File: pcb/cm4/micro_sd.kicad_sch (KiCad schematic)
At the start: 5 parts, among them J501 Micro_SD_Card, U501 RT9742GGJ5

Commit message: update pcb
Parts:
- C401: renamed from C501; footprint (none) -> Capacitor_SMD:C_0805_2012Metric
- C402: renamed from C502; footprint (none) -> Capacitor_SMD:C_0805_2012Metric
- J401: renamed from J501; footprint (none) -> Connector_Card:microSD_HC_Wuerth_693072010801
- R401: renamed from R501; footprint (none) -> Resistor_SMD:R_0805_2012Metric
- renumbered U501 to U401
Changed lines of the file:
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@@
 		(dnp no)
 		(fields_autoplaced yes)
-		(property "Reference" "#PWR0501"
+		(property "Reference" "#PWR0403"
 			(at 165.1 101.6 0)
 			(effects
@@
 			(project "cm4"
 				(path "/5d20b266-567e-45c6-9e3e-145c2aea1daa/8c670a00-fcb0-468c-ba79-62d0190039f0"
-					(reference "#PWR0501")
+					(reference "#PWR0403")
 					(unit 1)
 				)
@@
 		(dnp no)
 		(fields_autoplaced yes)
-		(property "Reference" "#PWR0505"
+		(property "Reference" "#PWR0406"
 			(at 213.36 102.87 0)
 			(effects
@@
 			(project "cm4"
 				(path "/5d20b266-567e-45c6-9e3e-145c2aea1daa/8c670a00-fcb0-468c-ba79-62d0190039f0"
-					(reference "#PWR0505")
+					(reference "#PWR0406")
 					(unit 1)
 				)
@@
 		(dnp no)
 		(fields_autoplaced yes)
-		(property "Reference" "J501"
+		(property "Reference" "J401"
 			(at 123.825 71.12 0)
 			(effects
@@
 			)
 		)
-		(property "Footprint" ""
+		(property "Footprint" "Connector_Card:microSD_HC_Wuerth_693072010801"
 			(at 152.4 82.55 0)
 			(effects
@@
 			)
 		)
+		(property "LCSC" ""
+			(at 123.19 90.17 0)
+			(effects
+				(font
+					(size 1.27 1.27)
+				)
+				(hide yes)
+			)
+		)
 		(pin "3"
 		)
@@
 			(project "cm4"
 				(path "/5d20b266-567e-45c6-9e3e-145c2aea1daa/8c670a00-fcb0-468c-ba79-62d0190039f0"
-					(reference "J501")
+					(reference "J401")
 					(unit 1)
 				)
@@
 		(dnp no)
 		(fields_autoplaced yes)
-		(property "Reference" "R501"
+		(property "Reference" "R401"
 			(at 177.8 87.6299 0)
 			(effects
@@
 			)
 		)
-		(property "Footprint" ""
+		(property "Footprint" "Resistor_SMD:R_0805_2012Metric"
 			(at 173.482 88.9 90)
 			(effects
@@
 			)
 		)
+		(property "LCSC" ""
+			(at 175.26 88.9 0)
+			(effects
+				(font
+					(size 1.27 1.27)
+				)
+				(hide yes)
+			)
+		)
 		(pin "2"
 		)
@@
 			(project "cm4"
 				(path "/5d20b266-567e-45c6-9e3e-145c2aea1daa/8c670a00-fcb0-468c-ba79-62d0190039f0"
-					(reference "R501")
+					(reference "R401")
 					(unit 1)
 				)
@@
 		(dnp no)
 		(fields_autoplaced yes)
-		(property "Reference" "C502"
+		(property "Reference" "C402"
 			(at 217.17 88.8999 0)
 			(effects
@@
 			)
 		)
-		(property "Footprint" ""
+		(property "Footprint" "Capacitor_SMD:C_0805_2012Metric"
 			(at 214.3252 93.98 0)
 			(effects
@@
 			)
 		)
+		(property "LCSC" ""
+			(at 213.36 90.17 0)
+			(effects
+				(font
+					(size 1.27 1.27)
+				)
+				(hide yes)
+			)
+		)
 		(pin "1"
 		)
@@
 			(project "cm4"
 				(path "/5d20b266-567e-45c6-9e3e-145c2aea1daa/8c670a00-fcb0-468c-ba79-62d0190039f0"
-					(reference "C502")
+					(reference "C402")
 					(unit 1)
 				)
@@
 		(dnp no)
 		(fields_autoplaced yes)
-		(property "Reference" "#PWR0502"
+		(property "Reference" "#PWR0401"
 			(at 99.06 110.49 0)
 			(effects
@@
 			(project "cm4"
 				(path "/5d20b266-567e-45c6-9e3e-145c2aea1daa/8c670a00-fcb0-468c-ba79-62d0190039f0"
-					(reference "#PWR0502")
+					(reference "#PWR0401")
 					(unit 1)
 				)
@@
 		(dnp no)
 		(fields_autoplaced yes)
-		(property "Reference" "U501"
+		(property "Reference" "U401"
 			(at 195.58 78.74 0)
 			(effects
@@
 			(project "cm4"
 				(path "/5d20b266-567e-45c6-9e3e-145c2aea1daa/8c670a00-fcb0-468c-ba79-62d0190039f0"
-					(reference "U501")
+					(reference "U401")
 					(unit 1)
 				)
@@
 		(dnp no)
 		(fields_autoplaced yes)
-		(property "Reference" "#PWR0504"
+		(property "Reference" "#PWR0405"
 			(at 195.58 105.41 0)
 			(effects
@@
 			(project "cm4"
 				(path "/5d20b266-567e-45c6-9e3e-145c2aea1daa/8c670a00-fcb0-468c-ba79-62d0190039f0"
-					(reference "#PWR0504")
+					(reference "#PWR0405")
 					(unit 1)
 				)
@@
 		(dnp no)
 		(fields_autoplaced yes)
-		(property "Reference" "#PWR0503"
+		(property "Reference" "#PWR0404"
 			(at 180.34 85.09 0)
 			(effects
@@
 			(project "cm4"
 				(path "/5d20b266-567e-45c6-9e3e-145c2aea1daa/8c670a00-fcb0-468c-ba79-62d0190039f0"
-					(reference "#PWR0503")
+					(reference "#PWR0404")
 					(unit 1)
 				)
@@
 		(dnp no)
 		(fields_autoplaced yes)
-		(property "Reference" "C501"
+		(property "Reference" "C401"
 			(at 168.91 87.6299 0)
 			(effects
@@
 			)
 		)
-		(property "Footprint" ""
+		(property "Footprint" "Capacitor_SMD:C_0805_2012Metric"
 			(at 166.0652 92.71 0)
 			(effects
@@
 			)
 		)
+		(property "LCSC" ""
+			(at 165.1 88.9 0)
+			(effects
+				(font
+					(size 1.27 1.27)
+				)
+				(hide yes)
+			)
+		)
 		(pin "1"
 		)
@@
 			(project "cm4"
 				(path "/5d20b266-567e-45c6-9e3e-145c2aea1daa/8c670a00-fcb0-468c-ba79-62d0190039f0"
-					(reference "C501")
+					(reference "C401")
 					(unit 1)
 				)
@@
 		(dnp no)
 		(fields_autoplaced yes)
-		(property "Reference" "#PWR0506"
+		(property "Reference" "#PWR0402"
 			(at 144.78 114.3 0)
 			(effects
@@
 			(project "cm4"
 				(path "/5d20b266-567e-45c6-9e3e-145c2aea1daa/8c670a00-fcb0-468c-ba79-62d0190039f0"
-					(reference "#PWR0506")
-					(unit 1)
-				)
+					(reference "#PWR0402")
+					(unit 1)
+				)

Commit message: update cm4 board
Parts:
- removed J401: Micro_SD_Card, Connector_Card:microSD_HC_Wuerth_693072010801, symbol Connector:Micro_SD_Card
- added MICRO_SD401: TF-01A, DF40C-100DS-0.4V_51_:TF-01A, symbol TF-01A:TF-01A
- U401: LCSC (none) -> C250547
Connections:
- net GND: now also MICRO_SD401.6 (VSS), MICRO_SD401.MP1 (SHIELD), MICRO_SD401.MP2 (SHIELD), MICRO_SD401.MP3 (SHIELD), MICRO_SD401.MP4 (SHIELD)
- net SD_CLK: now also MICRO_SD401.5 (CLK)
- net SD_CMD: now also MICRO_SD401.3 (CMD)
- net SD_DATA0: now also MICRO_SD401.7 (DAT0)
- net SD_DATA1: now also MICRO_SD401.8 (DAT1)
- net SD_DATA2: now also MICRO_SD401.1 (DAT2)
- net SD_DATA3: now also MICRO_SD401.2 (CD/DAT3)
- net SD_PWR: now also MICRO_SD401.4 (VDD)
- no-connect marks 1 -> 2

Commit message: cm4: update footprint library, add 3d files, update dimensions
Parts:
- MICRO_SD401: footprint DF40C-100DS-0.4V_51_:TF-01A -> PRJ:TF-01A
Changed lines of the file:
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@@
 	(label "SD_PWR"
 		(at 130.81 82.55 180)
-		(fields_autoplaced yes)
 		(effects
 			(font
@@
 	(label "SD_PWR"
 		(at 217.17 86.36 0)
-		(fields_autoplaced yes)
 		(effects
 			(font
@@
 		(shape input)
 		(at 176.53 97.79 270)
-		(fields_autoplaced yes)
 		(effects
 			(font
@@
 		(shape input)
 		(at 82.55 90.17 180)
-		(fields_autoplaced yes)
 		(effects
 			(font
@@
 		(shape input)
 		(at 82.55 95.25 180)
-		(fields_autoplaced yes)
 		(effects
 			(font
@@
 		(shape input)
 		(at 82.55 92.71 180)
-		(fields_autoplaced yes)
 		(effects
 			(font
@@
 		(shape input)
 		(at 82.55 97.79 180)
-		(fields_autoplaced yes)
 		(effects
 			(font
@@
 		(shape input)
 		(at 82.55 85.09 180)
-		(fields_autoplaced yes)
 		(effects
 			(font
@@
 		(shape input)
 		(at 82.55 82.55 180)
-		(fields_autoplaced yes)
 		(effects
 			(font
@@
 			)
 		)
-		(property "Footprint" "DF40C-100DS-0.4V_51_:TF-01A"
+		(property "Footprint" "PRJ:TF-01A"
 			(at 102.87 90.17 0)
 			(effects

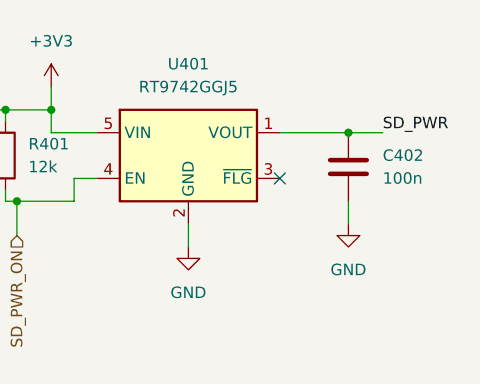
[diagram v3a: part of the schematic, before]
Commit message: add i2c
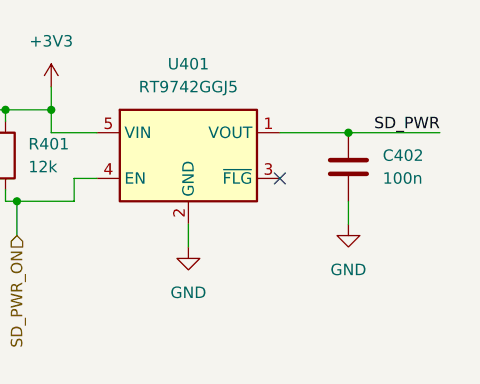
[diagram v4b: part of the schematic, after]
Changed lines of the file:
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@@
 	(wire
 		(pts
-			(xy 213.36 86.36) (xy 217.17 86.36)
+			(xy 213.36 86.36) (xy 223.52 86.36)
 		)
 		(stroke
@@
 	)
 	(label "SD_PWR"
-		(at 217.17 86.36 0)
+		(at 223.52 86.36 180)
 		(effects
 			(font
 				(size 1.27 1.27)
 			)
-			(justify left bottom)
-		)
-	)
+			(justify right bottom)
+		)
+	)

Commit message: update lscs fields
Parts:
- C401, C402: LCSC (none) -> C49678
- R401: LCSC (none) -> C17444
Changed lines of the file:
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@@
 			)
 		)
-		(property "LCSC" ""
+		(property "LCSC" "C17444"
 			(at 175.26 88.9 0)
 			(effects
@@
 			)
 		)
-		(property "LCSC" ""
+		(property "LCSC" "C49678"
 			(at 213.36 90.17 0)
 			(effects
@@
 			)
 		)
-		(property "LCSC" ""
+		(property "LCSC" "C49678"
 			(at 165.1 88.9 0)
 			(effects

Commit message: upgrade to kicad 9.0.0
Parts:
- MICRO_SD401: Availability (none) -> Not in stock; Check_prices (none) -> https://www.snapeda.com/parts/TF-01A/HRO+Electronics+Co.%25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; Description_1 (none) -> Standard Card Edge Connectors; MF (none) -> HRO Electronics Co., Ltd.; MP (none) -> TF-01A; Package (none) -> Package; Price (none) -> None; SnapEDA_Link (none) -> https://www.snapeda.com/parts/TF-01A/HRO+Electronics+Co.%25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
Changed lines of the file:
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@@
 (kicad_sch
-	(version 20231120)
+	(version 20250114)
 	(generator "eeschema")
-	(generator_version "8.0")
+	(generator_version "9.0")
 	(paper "A4")
 	(title_block
@@
 				(hide yes)
 			)
+		)
+		(property "MF" "HRO Electronics Co., Ltd."
+			(at 102.87 90.17 0)
+			(effects
+				(font
+					(size 1.27 1.27)
+				)
+				(justify bottom)
+				(hide yes)
+			)
+		)
+		(property "Description_1" "Standard Card Edge Connectors"
+			(at 102.87 90.17 0)
+			(effects
+				(font
+					(size 1.27 1.27)
+				)
+				(justify bottom)
+				(hide yes)
+			)
+		)
+		(property "Package" "Package"
+			(at 102.87 90.17 0)
+			(effects
+				(font
+					(size 1.27 1.27)
+				)
+				(justify bottom)
+				(hide yes)
+			)
+		)
+		(property "Price" "None"
+			(at 102.87 90.17 0)
+			(effects
+				(font
+					(size 1.27 1.27)
+				)
+				(justify bottom)
+				(hide yes)
+			)
+		)
+		(property "SnapEDA_Link" "https://www.snapeda.com/parts/TF-01A/HRO+Electronics+Co.%252C+Ltd./view-part/?ref=snap"
+			(at 102.87 90.17 0)
+			(effects
+				(font
+					(size 1.27 1.27)
+				)
+				(justify bottom)
+				(hide yes)
+			)
+		)
+		(property "MP" "TF-01A"
+			(at 102.87 90.17 0)
+			(effects
+				(font
+					(size 1.27 1.27)
+				)
+				(justify bottom)
+				(hide yes)
+			)
+		)
+		(property "Availability" "Not in stock"
+			(at 102.87 90.17 0)
+			(effects
+				(font
+					(size 1.27 1.27)
+				)
+				(justify bottom)
+				(hide yes)
+			)
+		)
+		(property "Check_prices" "https://www.snapeda.com/parts/TF-01A/HRO+Electronics+Co.%252C+Ltd./view-part/?ref=eda"
+			(at 102.87 90.17 0)
+			(effects
+				(font
+					(size 1.27 1.27)
+				)
+				(justify bottom)
+				(hide yes)
+			)

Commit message: update ALL parts
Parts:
- C401, C402: LCSC C49678 -> C28233
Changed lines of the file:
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@@
+			)
+		)
+		(property "MOUSER" ""
+			(at 175.26 88.9 0)
+			(effects
+				(font
+					(size 1.27 1.27)
+				)
 			)
 		)
@@
 			)
 		)
-		(property "LCSC" "C49678"
+		(property "LCSC" "C28233"
 			(at 213.36 90.17 0)
 			(effects
@@
 				)
 				(hide yes)
+			)
+		)
+		(property "MOUSER" ""
+			(at 213.36 90.17 0)
+			(effects
+				(font
+					(size 1.27 1.27)
+				)
 			)
 		)
@@
 			)
 		)
+		(property "MOUSER" ""
+			(at 195.58 88.9 0)
+			(effects
+				(font
+					(size 1.27 1.27)
+				)
+			)
+		)
 		(pin "1"
 		)
@@
 			)
 		)
-		(property "LCSC" "C49678"
+		(property "LCSC" "C28233"
 			(at 165.1 88.9 0)
 			(effects
@@
 				)
 				(hide yes)
+			)
+		)
+		(property "MOUSER" ""
+			(at 165.1 88.9 0)
+			(effects
+				(font
+					(size 1.27 1.27)
+				)
 			)
 		)
@@
 			)
 		)
+		(property "MOUSER" ""
+			(at 102.87 90.17 0)
+			(effects
+				(font
+					(size 1.27 1.27)
+				)
+			)
+		)
